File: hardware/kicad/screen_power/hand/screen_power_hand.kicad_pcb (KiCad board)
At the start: 2 copper layers, 68 x 76 mm, 41 parts, among them J1 AUX 5V INPUT, J101 PI USB / XH4, J102 TOUCH / XH4, J103 SCREEN 1 POWER, J2 GPIO17 / GND, J201 PI USB / XH4, J202 TOUCH / XH4, J203 SCREEN 2 POWER, K101 IM02TS, K201 IM02TS, Q1 2N3904, Q101 2N7000, Q2 2N3906, Q201 2N7000, Q3 SUP70101EL, Q4 SUP70101EL

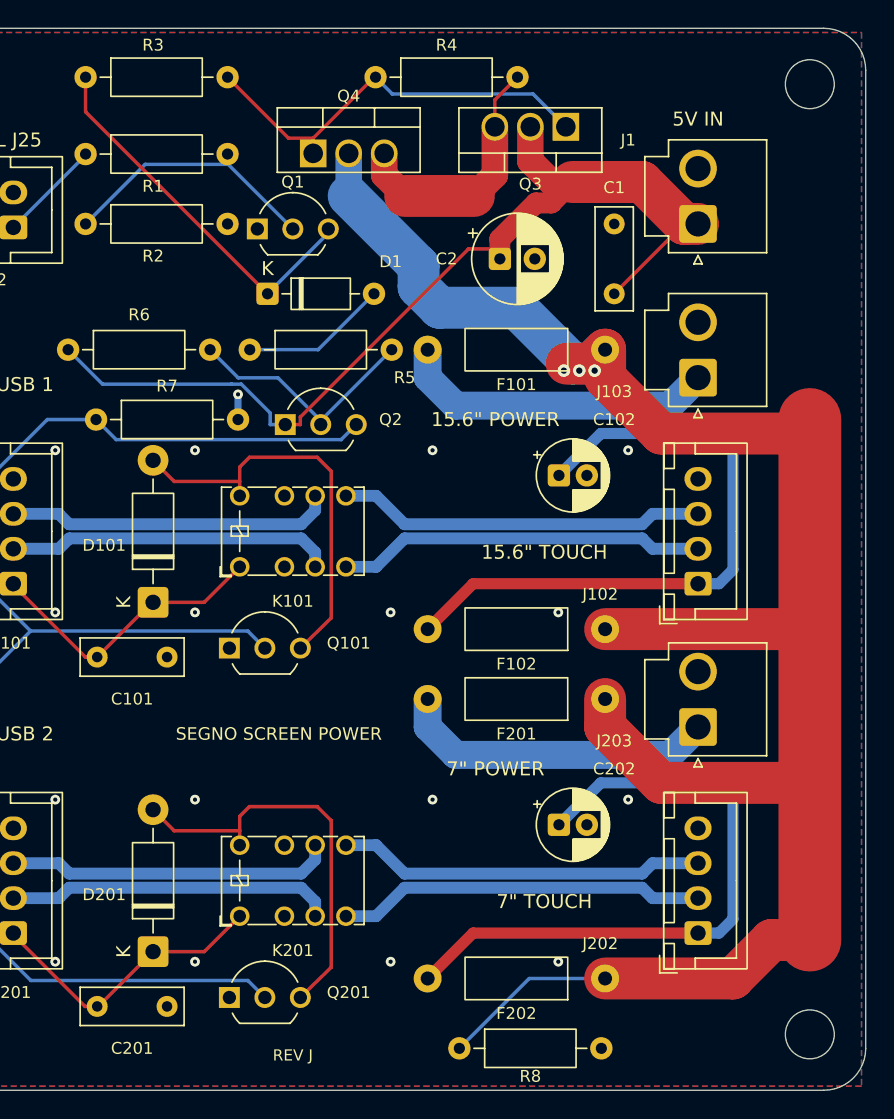
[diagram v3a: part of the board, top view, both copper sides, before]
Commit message: fix(hardware): finish screen power routing and assembly package
Finish the power-width transitions, correct capacitor models and mated-plug clearance, and align the wiring and aggregate power budget. Publish verified Revision K manufacturing files. Record completed local engineering reviews and incomplete Claude/OpenCode reviews caused by provider usage limits.
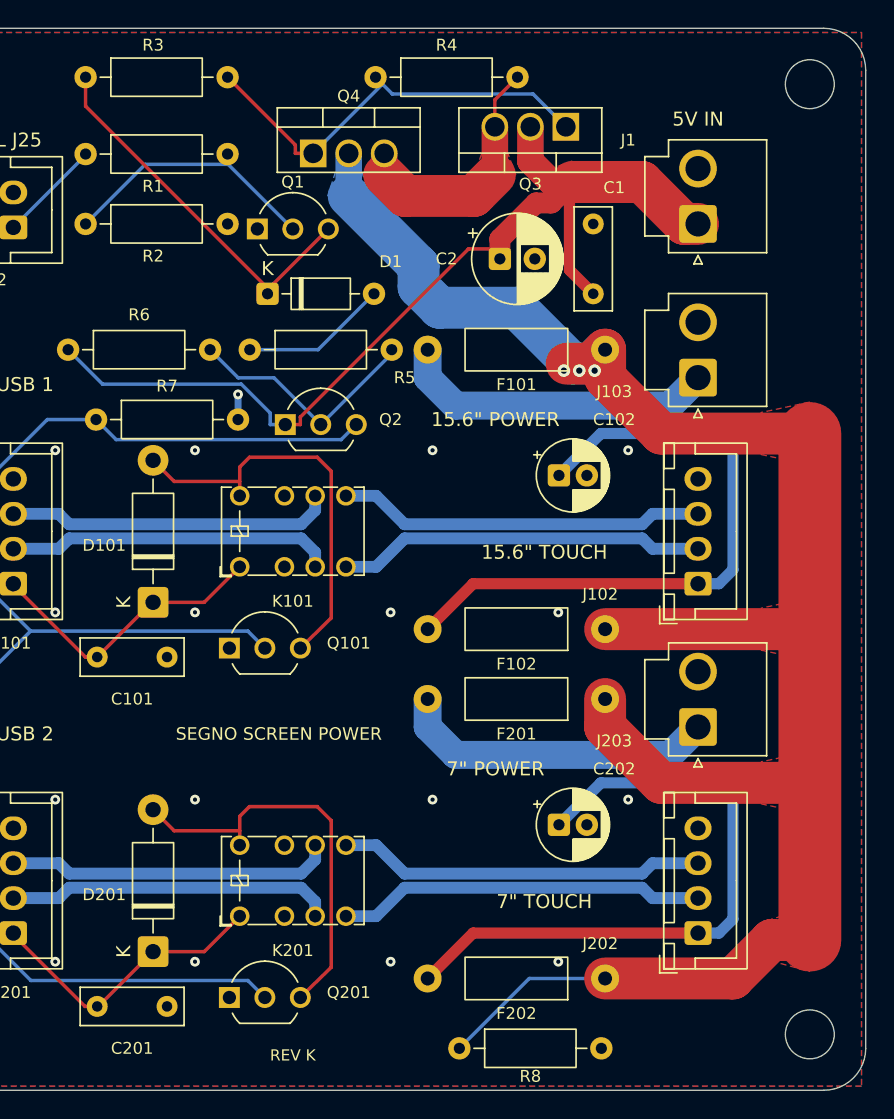
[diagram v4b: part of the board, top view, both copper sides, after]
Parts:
- moved C1 1.50 mm to (48.5, 19.0)
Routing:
- net AUX_5V: track 69.5 -> 72.5 mm
- net SWITCHED_5V: track 149.6 -> 148.6 mm
- added copper zone on F.Cu, net AUX_5V
- added copper zone on F.Cu, net COMMON_SOURCE
- added copper zone on B.Cu, net SWITCHED_5V
- added copper zone on F.Cu, net SWITCHED_5V
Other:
- board text added: "REV K"
- board text added: "SEGNO SCREEN POWER / REV K"
- board text removed: "REV J"
- board text removed: "SEGNO SCREEN POWER / REV J"
